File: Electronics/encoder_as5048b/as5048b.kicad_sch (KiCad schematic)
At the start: 16 parts, among them IC1 AS5048B-HTSP, J1 Conn_01x04_Male, J2 Conn_01x04_Male

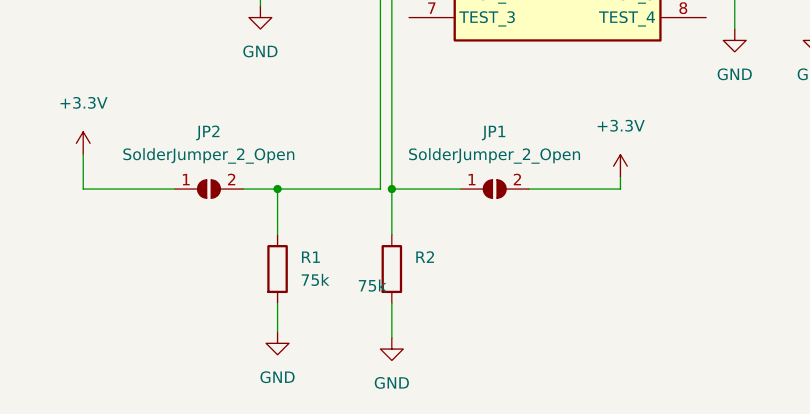
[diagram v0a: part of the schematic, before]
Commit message: Update encoder PCB. Add driver for INA226 power monitor chip.
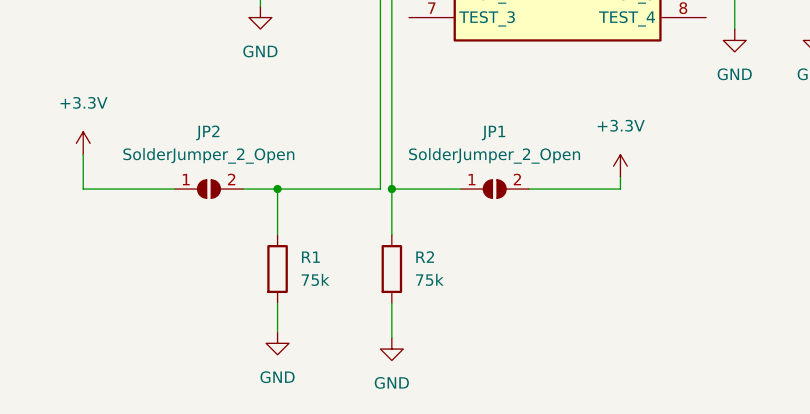
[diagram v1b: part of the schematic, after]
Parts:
- C1: RS 464-6688 -> 247-7824
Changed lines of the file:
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@@
       (effects (font (size 1.27 1.27)) hide)
     )
-    (property "RS" "    464-6688" (at 179.07 98.425 0)
+    (property "RS" "    247-7824" (at 179.07 98.425 0)
       (effects (font (size 1.27 1.27)) hide)
     )
@@
       (effects (font (size 1.27 1.27)) (justify left))
     )
-    (property "Value" "75k" (at 128.27 132.7149 0)
+    (property "Value" "75k" (at 134.62 132.08 0)
       (effects (font (size 1.27 1.27)) (justify left))
     )
